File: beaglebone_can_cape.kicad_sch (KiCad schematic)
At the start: 25 parts, among them J1 DCAN0, J2 DCAN1, J3 DTM15-12PA, J4 Conn_02x02_Top_Bottom, J5 Battery Harness, P8 BeagleBone_Black_Header, P9 BeagleBone_Black_Header, U1 TCAN332, U2 TCAN332, U3 LMR51430

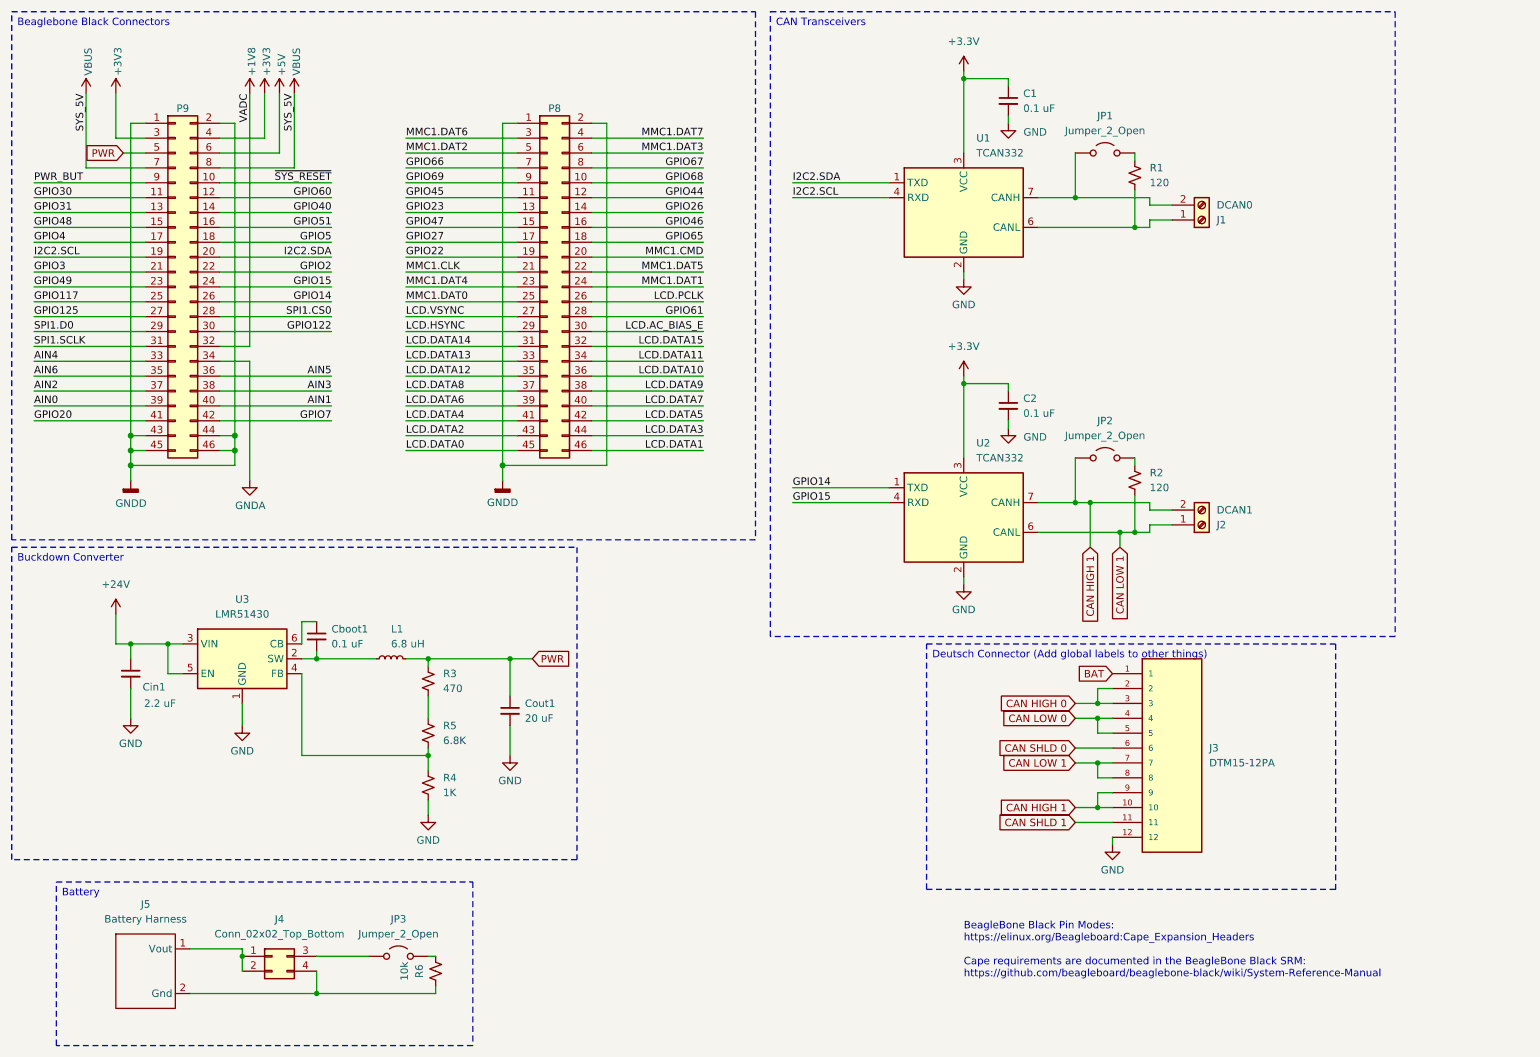
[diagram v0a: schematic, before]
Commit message: PCB Version 1: Before Week 4 Meeting
* Reorganized the board to support Deutsch
* Assigned all components to have footprints
* Simplified the schematic, namely the pins
* Created the battery circuit and put on PCB

Co-Authored-By: Zach Weidner <119375087+WeidnerZ@users.noreply.github.com>
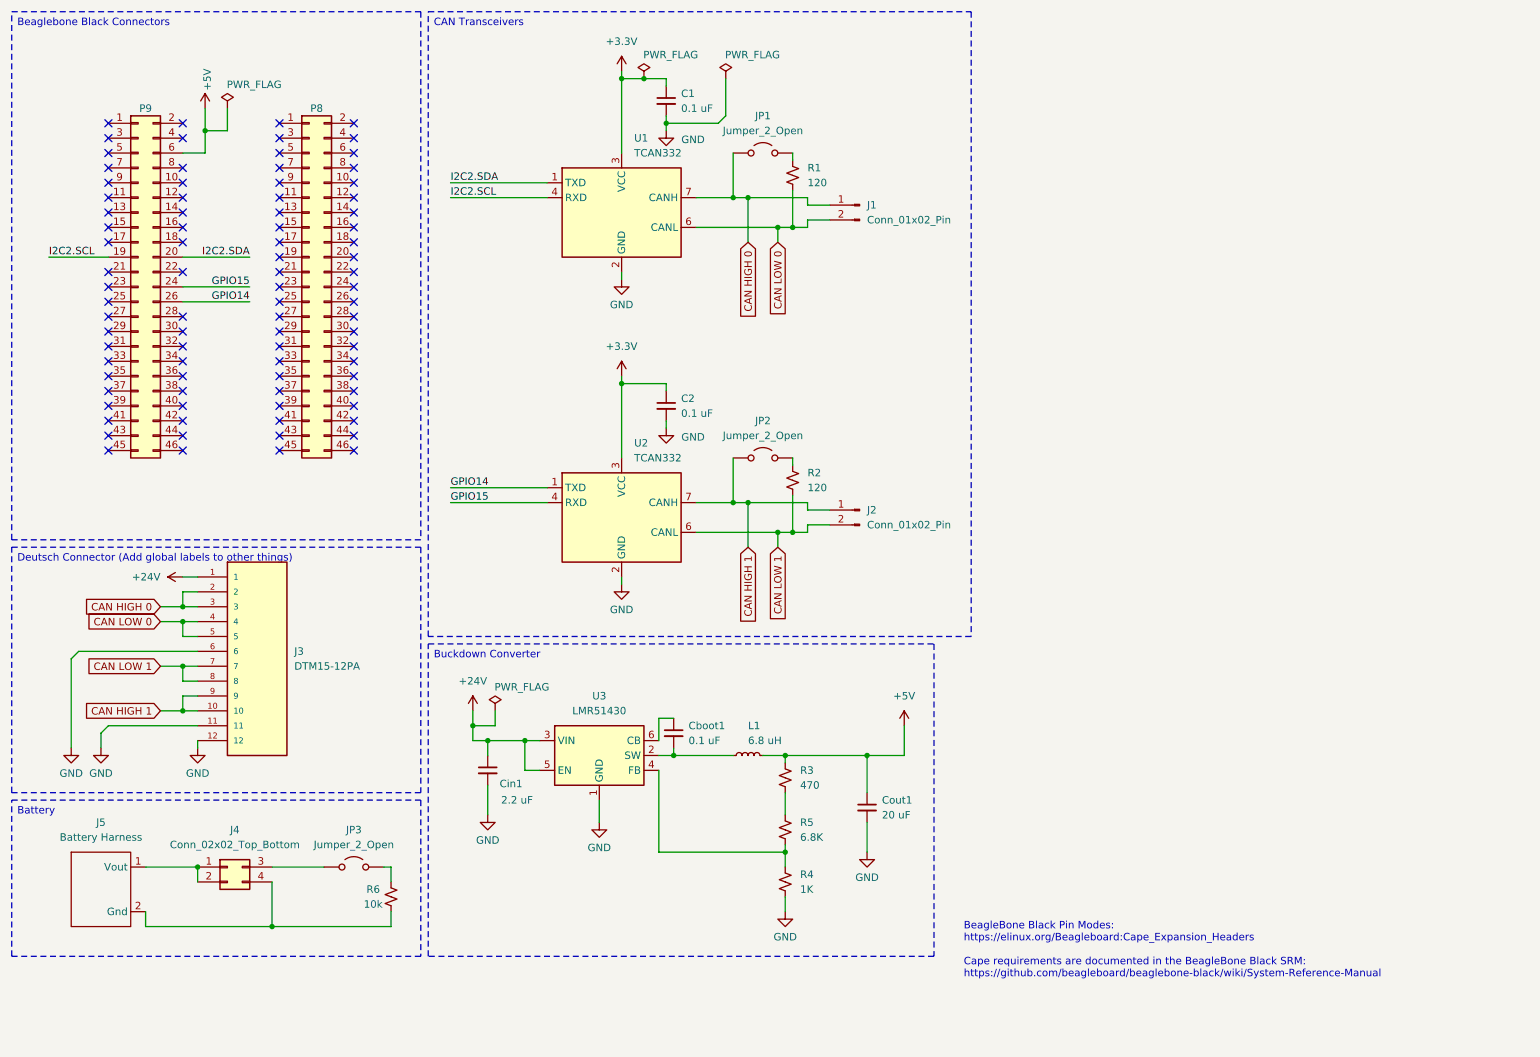
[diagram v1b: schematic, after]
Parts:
- removed J1: DCAN0, TerminalBlock_RND:TerminalBlock_RND_205-00232_1x02_P5.08mm_Horizontal, symbol Connector:Screw_Terminal_01x02
- removed J2: DCAN1, TerminalBlock_RND:TerminalBlock_RND_205-00232_1x02_P5.08mm_Horizontal, symbol Connector:Screw_Terminal_01x02
- added J1, J2: Conn_01x02_Pin, Connector_PinHeader_2.54mm:PinHeader_1x02_P2.54mm_Vertical, symbol Connector:Conn_01x02_Pin
- J3: footprint DTM15-12PA:TE_DTM15-12PA -> Senior Design:TE_DTM15-12PA
- JP3: footprint (none) -> Connector_PinHeader_2.54mm:PinHeader_1x02_P2.54mm_Vertical
- L1: footprint Inductor_SMD:L_0805_2012Metric -> Inductor_SMD:L_1210_3225Metric
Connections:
- net BAT is gone; now on net +24V: J3.1
- net CAN SHLD 0 is gone; now on net GND: J3.6
- net CAN SHLD 1 is gone; now on net GND: J3.11
- net +5V: now also Cout1.1, L1.2, R3.1
- net CAN HIGH 0: now also JP1.1 (A), U1.7 (CANH), J1.1 (Pin_1)
- net CAN HIGH 1: now also J2.1 (Pin_1)
- net CAN LOW 0: now also R1.2, U1.6 (CANL), J1.2 (Pin_2)
- net CAN LOW 1: now also J2.2 (Pin_2)
- net +1V8: no longer names the net of P9.32 (Pin_32)
- net +3V3: no longer names the net of P9.3 (Pin_3)
- net +3V3: no longer P9.4 (Pin_4)
- net AIN0: no longer names the net of P9.39 (Pin_39)
- net AIN1: no longer names the net of P9.40 (Pin_40)
- net AIN2: no longer names the net of P9.37 (Pin_37)
- net AIN3: no longer names the net of P9.38 (Pin_38)
- net AIN4: no longer names the net of P9.33 (Pin_33)
- net AIN5: no longer names the net of P9.36 (Pin_36)
- net AIN6: no longer names the net of P9.35 (Pin_35)
- net GNDA: no longer names the net of P9.34 (Pin_34)
- removed net GNDD: P8.1 (Pin_1), P8.2 (Pin_2), P9.1 (Pin_1), P9.2 (Pin_2), P9.43 (Pin_43), P9.44 (Pin_44), P9.45 (Pin_45), P9.46 (Pin_46)
- net GPIO117: no longer names the net of P9.25 (Pin_25)
- net GPIO122: no longer names the net of P9.30 (Pin_30)
- net GPIO125: no longer names the net of P9.27 (Pin_27)
- net GPIO2: no longer names the net of P9.22 (Pin_22)
- net GPIO20: no longer names the net of P9.41 (Pin_41)
- net GPIO22: no longer names the net of P8.19 (Pin_19)
- net GPIO23: no longer names the net of P8.13 (Pin_13)
- net GPIO26: no longer names the net of P8.14 (Pin_14)
- net GPIO27: no longer names the net of P8.17 (Pin_17)
- net GPIO3: no longer names the net of P9.21 (Pin_21)
- net GPIO30: no longer names the net of P9.11 (Pin_11)
- net GPIO31: no longer names the net of P9.13 (Pin_13)
- net GPIO4: no longer names the net of P9.17 (Pin_17)
- net GPIO40: no longer names the net of P9.14 (Pin_14)
- net GPIO44: no longer names the net of P8.12 (Pin_12)
- net GPIO45: no longer names the net of P8.11 (Pin_11)
- net GPIO46: no longer names the net of P8.16 (Pin_16)
- net GPIO47: no longer names the net of P8.15 (Pin_15)
- net GPIO48: no longer names the net of P9.15 (Pin_15)
- net GPIO49: no longer names the net of P9.23 (Pin_23)
- net GPIO5: no longer names the net of P9.18 (Pin_18)
- net GPIO51: no longer names the net of P9.16 (Pin_16)
- net GPIO60: no longer names the net of P9.12 (Pin_12)
- net GPIO61: no longer names the net of P8.28 (Pin_28)
- net GPIO65: no longer names the net of P8.18 (Pin_18)
- net GPIO66: no longer names the net of P8.7 (Pin_7)
- net GPIO67: no longer names the net of P8.8 (Pin_8)
- net GPIO68: no longer names the net of P8.10 (Pin_10)
- net GPIO69: no longer names the net of P8.9 (Pin_9)
- net GPIO7: no longer names the net of P9.42 (Pin_42)
- net LCD.AC_BIAS_E: no longer names the net of P8.30 (Pin_30)
- net LCD.DATA0: no longer names the net of P8.45 (Pin_45)
- net LCD.DATA1: no longer names the net of P8.46 (Pin_46)
- net LCD.DATA10: no longer names the net of P8.36 (Pin_36)
- net LCD.DATA11: no longer names the net of P8.34 (Pin_34)
- net LCD.DATA12: no longer names the net of P8.35 (Pin_35)
- net LCD.DATA13: no longer names the net of P8.33 (Pin_33)
- net LCD.DATA14: no longer names the net of P8.31 (Pin_31)
- net LCD.DATA15: no longer names the net of P8.32 (Pin_32)
- net LCD.DATA2: no longer names the net of P8.43 (Pin_43)
- net LCD.DATA3: no longer names the net of P8.44 (Pin_44)
- net LCD.DATA4: no longer names the net of P8.41 (Pin_41)
- net LCD.DATA5: no longer names the net of P8.42 (Pin_42)
- net LCD.DATA6: no longer names the net of P8.39 (Pin_39)
- net LCD.DATA7: no longer names the net of P8.40 (Pin_40)
- net LCD.DATA8: no longer names the net of P8.37 (Pin_37)
- net LCD.DATA9: no longer names the net of P8.38 (Pin_38)
- net LCD.HSYNC: no longer names the net of P8.29 (Pin_29)
- net LCD.PCLK: no longer names the net of P8.26 (Pin_26)
- net LCD.VSYNC: no longer names the net of P8.27 (Pin_27)
- net MMC1.CLK: no longer names the net of P8.21 (Pin_21)
- net MMC1.CMD: no longer names the net of P8.20 (Pin_20)
- net MMC1.DAT0: no longer names the net of P8.25 (Pin_25)
- net MMC1.DAT1: no longer names the net of P8.24 (Pin_24)
- net MMC1.DAT2: no longer names the net of P8.5 (Pin_5)
- net MMC1.DAT3: no longer names the net of P8.6 (Pin_6)
- net MMC1.DAT4: no longer names the net of P8.23 (Pin_23)
- net MMC1.DAT5: no longer names the net of P8.22 (Pin_22)
- net MMC1.DAT6: no longer names the net of P8.3 (Pin_3)
- net MMC1.DAT7: no longer names the net of P8.4 (Pin_4)
- removed net PWR: Cout1.1, L1.2, P9.5 (Pin_5), R3.1
- net PWR_BUT: no longer names the net of P9.9 (Pin_9)
- net SPI1.CS0: no longer names the net of P9.28 (Pin_28)
- net SPI1.D0: no longer names the net of P9.29 (Pin_29)
- net SPI1.SCLK: no longer names the net of P9.31 (Pin_31)
- net VBUS: no longer names the net of P9.7 (Pin_7)
- net VBUS: no longer P9.8 (Pin_8)
- net ~{SYS_RESET}: no longer names the net of P9.10 (Pin_10)
- no-connect marks 0 -> 87
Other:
- moved on the sheet: C1, C2, Cboot1, Cin1, Cout1, J3, J4, J5, JP1, JP2, JP3, L1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

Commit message: did I forget to push this before? oops
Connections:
- net GNDD: now reaches P9.1 (Pin_1)
- net GNDD: now also P8.1 (Pin_1), P8.2 (Pin_2), P9.2 (Pin_2), P9.43 (Pin_43), P9.44 (Pin_44), P9.45 (Pin_45), P9.46 (Pin_46)
- net +3V3: now reaches P9.3 (Pin_3)
- net +3V3: now also P9.4 (Pin_4)
- no-connect marks 87 -> 77

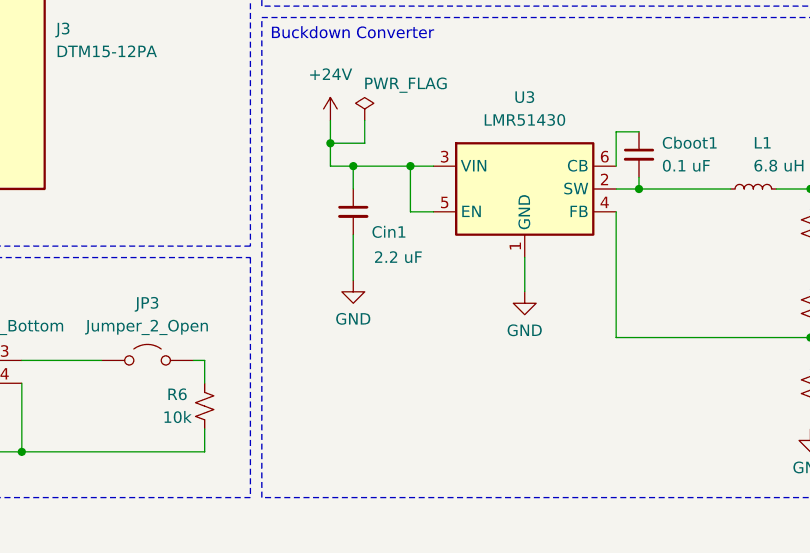
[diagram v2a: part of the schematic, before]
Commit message: pushing added TVS diode in schem, not wired in yet, working on footprint now
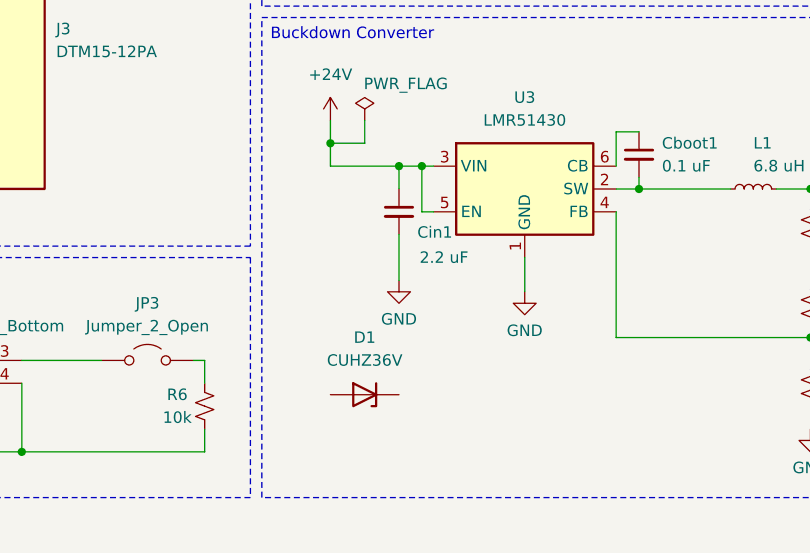
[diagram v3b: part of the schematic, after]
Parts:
- added D1: CUHZ36V, symbol Diode:PTVS5V0Z1USK
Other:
- moved on the sheet: Cin1
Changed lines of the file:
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@@
 	)
 	(junction
-		(at 102.87 139.7)
-		(diameter 0)
-		(color 0 0 0 0)
-	)
-	(junction
-		(at 96.52 139.7)
-		(diameter 0)
-		(color 0 0 0 0)
-	)
-	(junction
 		(at 44.45 116.84)
 		(diameter 0)
@@
 	)
 	(junction
+		(at 104.14 139.7)
+		(diameter 0)
+		(color 0 0 0 0)
+	)
+	(junction
+		(at 101.6 139.7)
+		(diameter 0)
+		(color 0 0 0 0)
+	)
+	(junction
 		(at 146.05 104.14)
 		(diameter 0)
@@
 	(wire
 		(pts
-			(xy 96.52 147.32) (xy 96.52 152.4)
+			(xy 101.6 147.32) (xy 101.6 152.4)
 		)
 		(stroke
@@
 	(wire
 		(pts
+			(xy 101.6 139.7) (xy 104.14 139.7)
+		)
+		(stroke
+			(width 0)
+			(type default)
+		)
+	)
+	(wire
+		(pts
 			(xy 151.13 102.87) (xy 151.13 104.14)
 		)
@@
 	(wire
 		(pts
-			(xy 102.87 139.7) (xy 102.87 144.78)
+			(xy 104.14 139.7) (xy 104.14 144.78)
 		)
 		(stroke
@@
 	(wire
 		(pts
-			(xy 96.52 139.7) (xy 93.98 139.7)
+			(xy 93.98 139.7) (xy 101.6 139.7)
 		)
 		(stroke
@@
 	(wire
 		(pts
-			(xy 102.87 139.7) (xy 105.41 139.7)
-		)
-		(stroke
-			(width 0)
-			(type default)
-		)
-	)
-	(wire
-		(pts
 			(xy 140.97 99.06) (xy 151.13 99.06)
 		)
@@
 	(wire
 		(pts
-			(xy 105.41 144.78) (xy 102.87 144.78)
+			(xy 105.41 144.78) (xy 104.14 144.78)
 		)
 		(stroke
@@
 	(wire
 		(pts
-			(xy 96.52 139.7) (xy 102.87 139.7)
-		)
-		(stroke
-			(width 0)
-			(type default)
-		)
-	)
-	(wire
-		(pts
 			(xy 161.29 142.24) (xy 161.29 148.59)
 		)
@@
 	(wire
 		(pts
-			(xy 96.52 139.7) (xy 96.52 142.24)
+			(xy 101.6 139.7) (xy 101.6 142.24)
 		)
 		(stroke
@@
 	(wire
 		(pts
+			(xy 104.14 139.7) (xy 105.41 139.7)
+		)
+		(stroke
+			(width 0)
+			(type default)
+		)
+	)
+	(wire
+		(pts
 			(xy 127 85.09) (xy 127 86.36)
 		)
@@
 	)
 	(symbol
+		(lib_id "Diode:PTVS5V0Z1USK")
+		(at 97.79 165.1 180)
+		(unit 1)
+		(exclude_from_sim no)
+		(in_bom yes)
+		(on_board yes)
+		(dnp no)
+		(fields_autoplaced yes)
+		(property "Reference" "D1"
+			(at 97.79 158.75 0)
+			(effects
+				(font
+					(size 1.27 1.27)
+				)
+			)
+		)
+		(property "Value" "CUHZ36V"
+			(at 97.79 161.29 0)
+			(effects
+				(font
+					(size 1.27 1.27)
+				)
+			)
+		)
+		(property "Footprint" ""
+			(at 97.79 160.655 0)
+			(effects
+				(font
+					(size 1.27 1.27)
+				)
+				(hide yes)
+			)
+		)
+		(property "Datasheet" "https://toshiba.semicon-storage.com/info/CUHZ36V_datasheet_en_20210917.pdf?did=70664&prodName=CUHZ36V"
+			(at 97.79 165.1 0)
+			(effects
+				(font
+					(size 1.27 1.27)
+				)
+				(hide yes)
+			)
+		)
+		(property "Description" ""
+			(at 97.79 165.1 0)
+			(effects
+				(font
+					(size 1.27 1.27)
+				)
+				(hide yes)
+			)
+		)
+		(pin "1"
+		)
+		(pin "2"
+		)
+		(instances
+			(project ""
+				(path "/e63e39d7-6ac0-4ffd-8aa3-1841a4541b55"
+					(reference "D1")
+					(unit 1)
+				)
+			)
+		)
+	)
+	(symbol
 		(lib_id "power:PWR_FLAG")
 		(at 97.79 134.62 0)
@@
 	(symbol
 		(lib_id "Device:C_Small")
-		(at 96.52 144.78 0)
+		(at 101.6 144.78 0)
 		(unit 1)
 		(exclude_from_sim no)
@@
 		(dnp no)
 		(property "Reference" "Cin1"
-			(at 98.552 147.066 0)
+			(at 103.632 147.066 0)
 			(effects
 				(font
@@
 		)
 		(property "Value" "2.2 uF"
-			(at 98.806 149.86 0)
+			(at 103.886 149.86 0)
 			(effects
 				(font
@@
 		)
 		(property "Footprint" "Capacitor_SMD:C_0805_2012Metric"
-			(at 96.52 144.78 0)
+			(at 101.6 144.78 0)
 			(effects
 				(font
@@
 		)
 		(property "Datasheet" "~"
-			(at 96.52 144.78 0)
+			(at 101.6 144.78 0)
 			(effects
 				(font
@@
 		)
 		(property "Description" "Unpolarized capacitor, small symbol"
-			(at 96.52 144.78 0)
+			(at 101.6 144.78 0)
 			(effects
 				(font
@@
 	(symbol
 		(lib_id "power:GND")
-		(at 96.52 152.4 0)
+		(at 101.6 152.4 0)
 		(unit 1)
 		(exclude_from_sim no)
@@
 		(dnp no)
 		(property "Reference" "#PWR015"
-			(at 96.52 158.75 0)
+			(at 101.6 158.75 0)
 			(effects
 				(font
@@
 		)
 		(property "Value" "GND"
-			(at 96.52 156.718 0)
+			(at 101.6 156.718 0)
 			(effects
 				(font
@@
 		)
 		(property "Footprint" ""
-			(at 96.52 152.4 0)
+			(at 101.6 152.4 0)
 			(effects
 				(font
@@
 		)
 		(property "Datasheet" ""
-			(at 96.52 152.4 0)
+			(at 101.6 152.4 0)
 			(effects
 				(font
@@
 		)
 		(property "Description" "Power symbol creates a global label with name \"GND\" , ground"
-			(at 96.52 152.4 0)
+			(at 101.6 152.4 0)
 			(effects
 				(font

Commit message: pushing footprint assignment on schem
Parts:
- D1: footprint (none) -> SeniorDesign:TVSDiode
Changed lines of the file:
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@@
 			)
 		)
-		(property "Footprint" ""
+		(property "Footprint" "SeniorDesign:TVSDiode"
 			(at 97.79 160.655 0)
 			(effects
